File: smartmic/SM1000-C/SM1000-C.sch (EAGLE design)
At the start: 175 parts, among them CN1 HDR100-3, CN10 MJ-3523-SMT, CN11 HDR100-3, CN12 DF11-16DS, CN2 MOLEX-MINI-B-SMT, CN3 RASM712PX, CN4 RJ-45, CN5 MJ-3523-SMT, CN6 MJ-3523-SMT, CN7 MJ-3523-SMT, CN8 MJ-3523-SMT, CN9 MJ-3523-SMT, J1 JMP-2PIN, J3 JMP-2PIN, J4 JMP-2PIN, J5 JMP-2PIN, P1 TPAD50, P10 TPAD50, P11 TPAD50, P12 TPAD50, P13 TPAD50, P14 TPAD50, P15 TPAD50, P16 TPAD50, P17 TPAD50, P18 TPAD50, P19 TPAD50, P2 TPAD50, P20 TPAD50, P3 TPAD50, P4 TPAD50, P5 TPAD50, P6 TPAD50, P7 TPAD50, P8 TPAD50, P9 TPAD50, SW1 SW-BOURNS-7914S, SW2 SW-BOURNS-7914S, SW3 DPDT, SW4 SW-BOURNS-7914S, T1 SM-LP-5001, T2 SM-LP-5001, U1 STM32F405, U2 LD3985M33R, U3 STMPS2141, U4 EMIF02-USB03F2, U5 TPS54329E, U6 LMV341, U7 LMV341, U8 LM386M-1, U9 LMV341

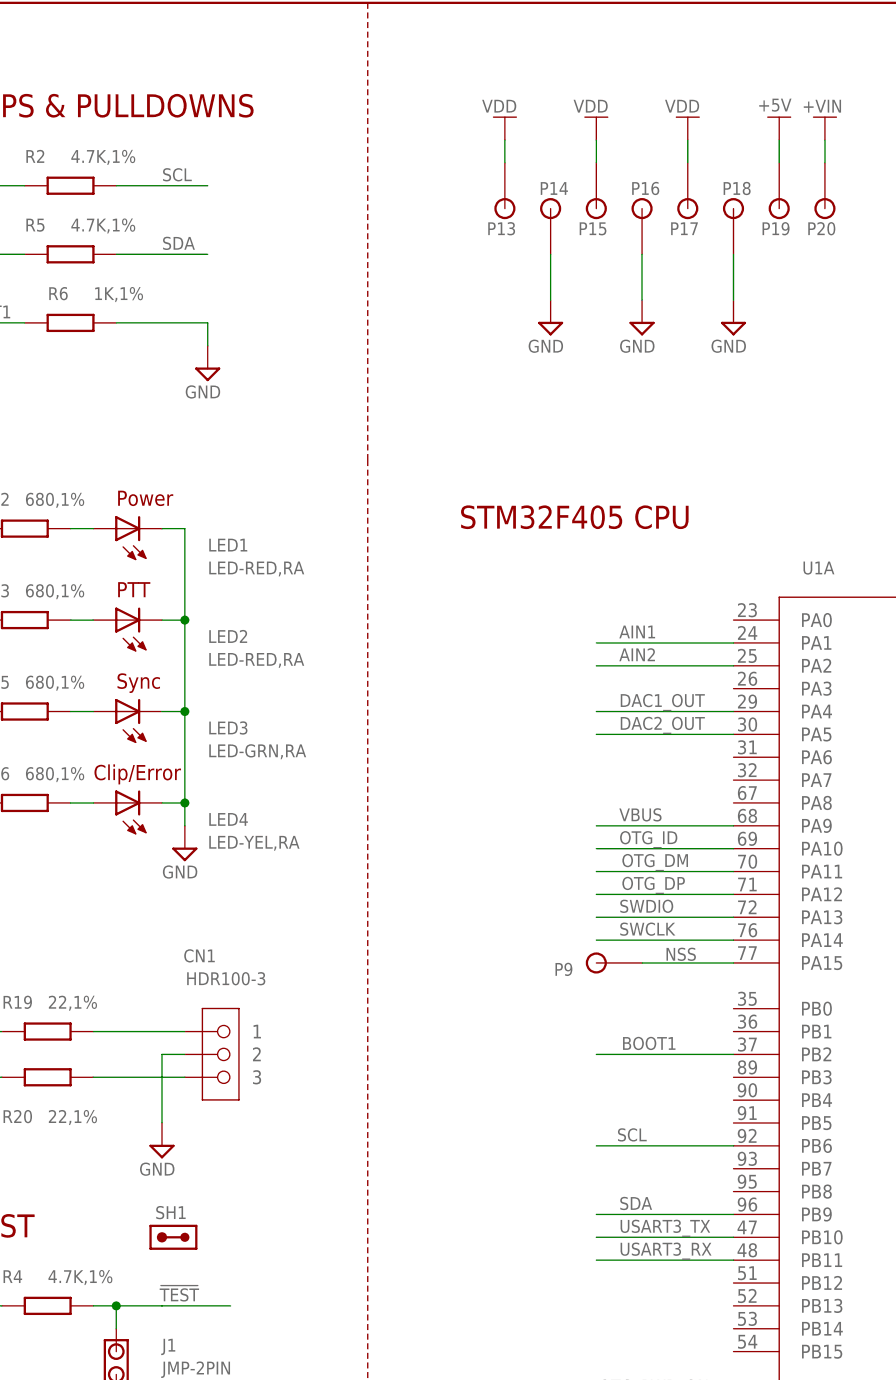
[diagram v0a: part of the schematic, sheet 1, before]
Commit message: Verifying Change-Log-C items 1-15 RGB
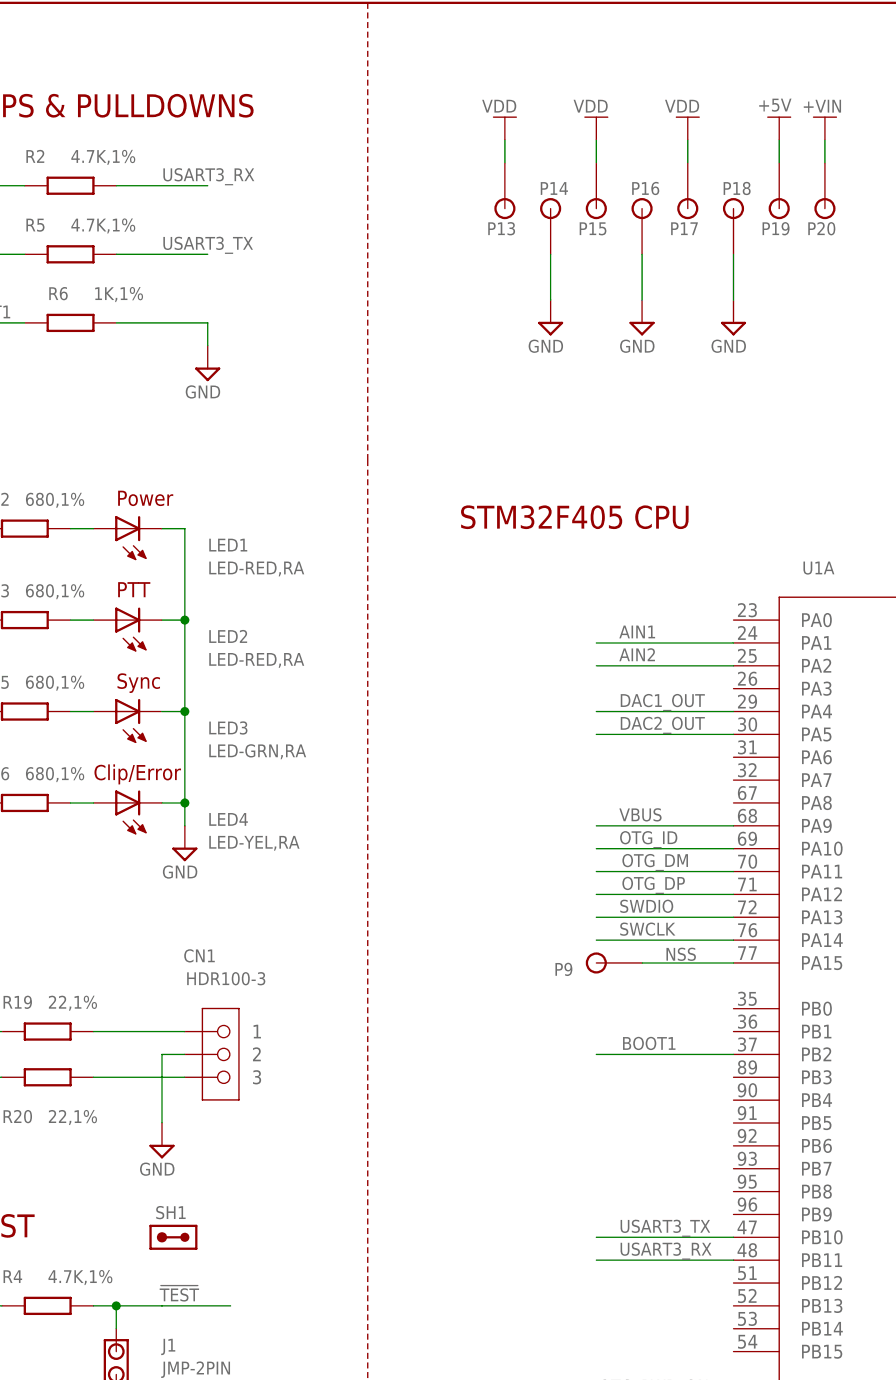
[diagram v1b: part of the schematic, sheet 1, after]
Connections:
- removed net SCL: R2.2, U1A.PB6
- removed net SDA: R5.2, U1A.PB9
- net USART3_RX: now also R2.2
- net USART3_TX: now also R5.2
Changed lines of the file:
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@@
-</segment>
-</net>
-<net name="SCL" class="0">
-<segment>
-<wire x1="104.14" y1="152.4" x2="88.9" y2="152.4" width="0.1524" layer="91"/>
-<label x="91.186" y="152.908" size="1.4224" layer="95" ratio="10"/>
-<pinref part="U1" gate="A" pin="PB6"/>
-</segment>
-<segment>
-<pinref part="R2" gate="G$1" pin="2"/>
-<wire x1="35.56" y1="259.08" x2="45.72" y2="259.08" width="0.1524" layer="91"/>
-<label x="40.64" y="259.588" size="1.4224" layer="95" ratio="10"/>
-</segment>
-</net>
-<net name="SDA" class="0">
-<segment>
-<wire x1="104.14" y1="144.78" x2="88.9" y2="144.78" width="0.1524" layer="91"/>
-<label x="91.44" y="145.288" size="1.4224" layer="95" ratio="10"/>
-<pinref part="U1" gate="A" pin="PB9"/>
-</segment>
-<segment>
-<pinref part="R5" gate="G$1" pin="2"/>
-<wire x1="35.56" y1="251.46" x2="45.72" y2="251.46" width="0.1524" layer="91"/>
-<label x="40.64" y="251.968" size="1.4224" layer="95" ratio="10"/>
 </segment>
 </net>
@@
 <label x="91.44" y="140.208" size="1.4224" layer="95" ratio="10"/>
 </segment>
+<segment>
+<pinref part="R2" gate="G$1" pin="2"/>
+<wire x1="35.56" y1="259.08" x2="45.72" y2="259.08" width="0.1524" layer="91"/>
+<label x="40.64" y="259.588" size="1.4224" layer="95" ratio="10"/>
+</segment>
 </net>
 <net name="USART3_TX" class="0">
@@
 <label x="91.44" y="142.748" size="1.4224" layer="95" ratio="10"/>
 </segment>
-</net>
+<segment>
+<pinref part="R5" gate="G$1" pin="2"/>
+<wire x1="35.56" y1="251.46" x2="45.72" y2="251.46" width="0.1524" layer="91"/>
+<label x="40.64" y="251.968" size="1.4224" layer="95" ratio="10"/>
+</segment>
+</net>

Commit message: Update to reflect review of Change-Log-C.txt  RGB 09/08/2014
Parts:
- added C54: 1nF,16V, AA-ipc-7351-capacitor:CAPACITOR_0603
- added R23: 10K,1%, AA-ipc-7351-resistor:RESISTOR_0603
- R39: value 22.1K,1% -> 2.21K,1%
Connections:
- removed net N$81: R47.3, R49.2
- new net N$13: R47.1, R49.2
- new net N$14: R23.2, R43.1, U6.-IN
- net AIN1: now also R23.1; no longer R43.1, U6.-IN
- net AIN2: now also C54.2, R42.1; no longer R42.3
- net N$41: now also C54.1, R42.3; no longer R42.1
- net N$82: now also R47.3; no longer R47.1
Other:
- moved on the sheet: P4, R47
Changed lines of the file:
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@@
 <part name="V56" library="A-SUPPLY2" deviceset="GND" device=""/>
 <part name="C34" library="AA-ipc-7351-capacitor" deviceset="CAPACITOR_" device="0603" value="1nF,25V"/>
-<part name="R39" library="AA-ipc-7351-resistor" deviceset="RESISTOR_" device="0603" value="22.1K,1%"/>
+<part name="R39" library="AA-ipc-7351-resistor" deviceset="RESISTOR_" device="0603" value="2.21K,1%"/>
 <part name="R40" library="AA-ipc-7351-resistor" deviceset="RESISTOR_" device="0603" value="2.2K,1%"/>
 <part name="V59" library="A-SUPPLY2" deviceset="GND" device=""/>
@@
 <part name="R22" library="AA-ipc-7351-resistor" deviceset="RESISTOR_" device="0603" value="22.1K,1%"/>
 <part name="V125" library="A-SUPPLY2" deviceset="GND" device=""/>
+<part name="C54" library="AA-ipc-7351-capacitor" deviceset="CAPACITOR_" device="0603" value="1nF,16V"/>
+<part name="R23" library="AA-ipc-7351-resistor" deviceset="RESISTOR_" device="0603" value="10K,1%"/>
 </parts>
 <sheets>
@@
 </instance>
 <instance part="B-FRAME3" gate="G$3" x="355.6" y="279.4" smashed="yes"/>
-<instance part="R47" gate="G$1" x="238.76" y="88.9" smashed="yes">
-<attribute name="NAME" x="233.68" y="86.36" size="1.4224" layer="95" ratio="9" rot="R90"/>
-<attribute name="VALUE" x="236.22" y="86.36" size="1.4224" layer="96" ratio="9" rot="R90"/>
+<instance part="R47" gate="G$1" x="238.76" y="88.9" smashed="yes" rot="MR180">
+<attribute name="NAME" x="233.68" y="91.44" size="1.4224" layer="95" ratio="9" rot="MR270"/>
+<attribute name="VALUE" x="236.22" y="91.44" size="1.4224" layer="96" ratio="9" rot="MR270"/>
 </instance>
 <instance part="R52" gate="G$1" x="226.06" y="132.08" smashed="yes" rot="R180">
@@
 <attribute name="VALUE" x="93.98" y="134.62" size="1.4224" layer="96" ratio="9"/>
 </instance>
-<instance part="R42" gate="G$1" x="116.84" y="147.32" smashed="yes" rot="R90">
-<attribute name="NAME" x="124.46" y="152.4" size="1.4224" layer="95" ratio="9"/>
-<attribute name="VALUE" x="124.46" y="149.86" size="1.4224" layer="96" ratio="9"/>
+<instance part="R42" gate="G$1" x="116.84" y="147.32" smashed="yes" rot="MR90">
+<attribute name="NAME" x="114.3" y="157.48" size="1.4224" layer="95" ratio="9" rot="MR0"/>
+<attribute name="VALUE" x="114.3" y="152.4" size="1.4224" layer="96" ratio="9" rot="MR0"/>
 </instance>
 <instance part="V62" gate="GND" x="99.06" y="109.22" smashed="yes">
@@
 <instance part="P2" gate="G$1" x="170.18" y="83.82" rot="R180"/>
 <instance part="P3" gate="G$1" x="27.94" y="71.12"/>
-<instance part="P4" gate="G$1" x="129.54" y="127" rot="R180"/>
+<instance part="P4" gate="G$1" x="132.08" y="127" rot="R180"/>
 <instance part="C1" gate="G$1" x="101.6" y="251.46" smashed="yes" rot="R90">
 <attribute name="NAME" x="96.52" y="266.7" size="1.4224" layer="95"/>
@@
 <attribute name="VALUE" x="25.4" y="47.498" size="1.4224" layer="96" ratio="9"/>
 </instance>
+<instance part="C54" gate="G$1" x="124.46" y="154.94" smashed="yes">
+<attribute name="NAME" x="127" y="157.48" size="1.4224" layer="95"/>
+<attribute name="VALUE" x="121.92" y="149.86" size="1.4224" layer="96"/>
+</instance>
+<instance part="R23" gate="G$1" x="187.96" y="147.32" smashed="yes">
+<attribute name="NAME" x="182.88" y="149.86" size="1.4224" layer="95" ratio="9"/>
+<attribute name="VALUE" x="187.96" y="149.86" size="1.4224" layer="96" ratio="9"/>
+</instance>
 </instances>
 <busses>
@@
 <segment>
 <label x="132.588" y="130.302" size="1.4224" layer="95" ratio="10"/>
-<wire x1="129.54" y1="129.54" x2="137.16" y2="129.54" width="0.1524" layer="91"/>
+<wire x1="132.08" y1="129.54" x2="137.16" y2="129.54" width="0.1524" layer="91"/>
 <pinref part="U9" gate="G$1" pin="OUT"/>
-<wire x1="124.46" y1="129.54" x2="129.54" y2="129.54" width="0.1524" layer="91"/>
-<pinref part="R42" gate="G$1" pin="3"/>
-<wire x1="124.46" y1="147.32" x2="129.54" y2="147.32" width="0.1524" layer="91"/>
-<wire x1="129.54" y1="147.32" x2="129.54" y2="129.54" width="0.1524" layer="91"/>
-<wire x1="129.54" y1="127" x2="129.54" y2="129.54" width="0.1524" layer="91"/>
+<wire x1="124.46" y1="129.54" x2="132.08" y2="129.54" width="0.1524" layer="91"/>
+<wire x1="132.08" y1="147.32" x2="132.08" y2="129.54" width="0.1524" layer="91"/>
+<wire x1="132.08" y1="127" x2="132.08" y2="129.54" width="0.1524" layer="91"/>
 <pinref part="P4" gate="G$1" pin="1"/>
-<junction x="129.54" y="129.54"/>
+<junction x="132.08" y="129.54"/>
+<pinref part="C54" gate="G$1" pin="2"/>
+<wire x1="129.54" y1="154.94" x2="132.08" y2="154.94" width="0.1524" layer="91"/>
+<wire x1="132.08" y1="154.94" x2="132.08" y2="147.32" width="0.1524" layer="91"/>
+<pinref part="R42" gate="G$1" pin="1"/>
+<wire x1="124.46" y1="147.32" x2="132.08" y2="147.32" width="0.1524" layer="91"/>
+<junction x="132.08" y="147.32"/>
 </segment>
 </net>
@@
 <wire x1="177.8" y1="129.54" x2="170.18" y2="129.54" width="0.1524" layer="91"/>
 <wire x1="170.18" y1="127" x2="170.18" y2="129.54" width="0.1524" layer="91"/>
-<pinref part="U6" gate="G$1" pin="-IN"/>
-<wire x1="193.04" y1="132.08" x2="195.58" y2="132.08" width="0.1524" layer="91"/>
-<pinref part="R43" gate="G$1" pin="1"/>
-<wire x1="195.58" y1="132.08" x2="198.12" y2="132.08" width="0.1524" layer="91"/>
-<wire x1="195.58" y1="132.08" x2="195.58" y2="147.32" width="0.1524" layer="91"/>
-<wire x1="195.58" y1="147.32" x2="170.18" y2="147.32" width="0.1524" layer="91"/>
-<junction x="195.58" y="132.08"/>
 <wire x1="170.18" y1="129.54" x2="170.18" y2="147.32" width="0.1524" layer="91"/>
 <pinref part="P1" gate="G$1" pin="1"/>
 <junction x="170.18" y="129.54"/>
+<pinref part="R23" gate="G$1" pin="1"/>
+<wire x1="170.18" y1="147.32" x2="182.88" y2="147.32" width="0.1524" layer="91"/>
 </segment>
 </net>
@@
 </segment>
 </net>
-<net name="N$81" class="0">
-<segment>
-<pinref part="R49" gate="G$1" pin="2"/>
-<pinref part="R47" gate="G$1" pin="3"/>
-<wire x1="238.76" y1="78.74" x2="238.76" y2="81.28" width="0.1524" layer="91"/>
-</segment>
-</net>
 <net name="N$82" class="0">
 <segment>
-<pinref part="R47" gate="G$1" pin="1"/>
-<wire x1="238.76" y1="96.52" x2="238.76" y2="99.06" width="0.1524" layer="91"/>
 <pinref part="R48" gate="G$1" pin="1"/>
 <wire x1="238.76" y1="99.06" x2="236.22" y2="99.06" width="0.1524" layer="91"/>
+<pinref part="R47" gate="G$1" pin="3"/>
+<wire x1="238.76" y1="96.52" x2="238.76" y2="99.06" width="0.1524" layer="91"/>
 </segment>
 </net>
@@
 </segment>
 </net>
-<net name="N$61" class="0">
-<segment>
-<pinref part="R47" gate="G$1" pin="2"/>
-<pinref part="C47" gate="G$1" pin="1"/>
-<wire x1="243.84" y1="88.9" x2="246.38" y2="88.9" width="0.1524" layer="91"/>
-</segment>
-</net>
 <net name="N$79" class="0">
 <segment>
@@
 <net name="N$41" class="0">
 <segment>
-<wire x1="106.68" y1="147.32" x2="109.22" y2="147.32" width="0.1524" layer="91"/>
-<pinref part="R42" gate="G$1" pin="1"/>
-<pinref part="R42" gate="G$1" pin="2"/>
-<wire x1="116.84" y1="152.4" x2="116.84" y2="154.94" width="0.1524" layer="91"/>
 <wire x1="116.84" y1="154.94" x2="106.68" y2="154.94" width="0.1524" layer="91"/>
 <wire x1="106.68" y1="154.94" x2="106.68" y2="147.32" width="0.1524" layer="91"/>
 <pinref part="R53" gate="G$1" pin="2"/>
 <wire x1="106.68" y1="144.78" x2="106.68" y2="147.32" width="0.1524" layer="91"/>
+<pinref part="C54" gate="G$1" pin="1"/>
+<wire x1="116.84" y1="154.94" x2="119.38" y2="154.94" width="0.1524" layer="91"/>
+<pinref part="R42" gate="G$1" pin="2"/>
+<wire x1="116.84" y1="152.4" x2="116.84" y2="154.94" width="0.1524" layer="91"/>
+<pinref part="R42" gate="G$1" pin="3"/>
+<wire x1="109.22" y1="147.32" x2="106.68" y2="147.32" width="0.1524" layer="91"/>
 <junction x="106.68" y="147.32"/>
+<junction x="116.84" y="154.94"/>
 </segment>
 </net>
@@
 </segment>
 </net>
+<net name="N$11" class="0">
+<segment>
+<pinref part="R47" gate="G$1" pin="2"/>
+<pinref part="C47" gate="G$1" pin="1"/>
+<wire x1="243.84" y1="88.9" x2="246.38" y2="88.9" width="0.1524" layer="91"/>
+</segment>
+</net>
+<net name="N$13" class="0">
+<segment>
+<pinref part="R47" gate="G$1" pin="1"/>
+<pinref part="R49" gate="G$1" pin="2"/>
+<wire x1="238.76" y1="81.28" x2="238.76" y2="78.74" width="0.1524" layer="91"/>
+</segment>
+</net>
+<net name="N$14" class="0">
+<segment>
+<pinref part="R43" gate="G$1" pin="1"/>
+<wire x1="195.58" y1="132.08" x2="198.12" y2="132.08" width="0.1524" layer="91"/>
+<wire x1="195.58" y1="132.08" x2="195.58" y2="147.32" width="0.1524" layer="91"/>
+<junction x="195.58" y="132.08"/>
+<pinref part="U6" gate="G$1" pin="-IN"/>
+<wire x1="193.04" y1="132.08" x2="195.58" y2="132.08" width="0.1524" layer="91"/>
+<pinref part="R23" gate="G$1" pin="2"/>
+<wire x1="193.04" y1="147.32" x2="195.58" y2="147.32" width="0.1524" layer="91"/>
+</segment>
+</net>

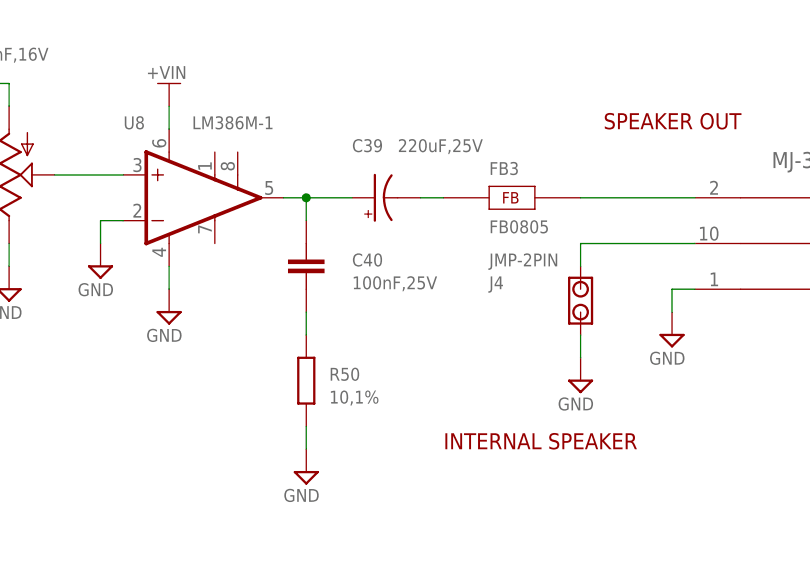
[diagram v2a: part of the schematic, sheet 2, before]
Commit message: Update SNN with Change-Log-C.txt changes. RGB 09/10/2014
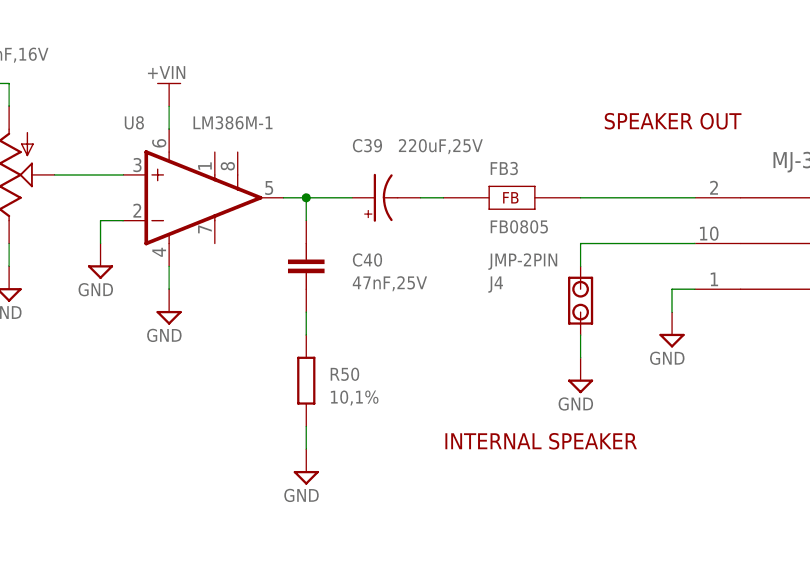
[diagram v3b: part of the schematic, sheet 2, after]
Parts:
- C40: value 100nF,25V -> 47nF,25V
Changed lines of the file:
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@@
 <part name="V64" library="A-SUPPLY2" deviceset="GND" device=""/>
 <part name="U$8" library="A-SUPPLY2" deviceset="+VIN" device=""/>
-<part name="C40" library="AA-ipc-7351-capacitor" deviceset="CAPACITOR_" device="0603" value="100nF,25V"/>
+<part name="C40" library="AA-ipc-7351-capacitor" deviceset="CAPACITOR_" device="0603" value="47nF,25V"/>
 <part name="R50" library="AA-ipc-7351-resistor" deviceset="RESISTOR_" device="0603" value="10,1%"/>
 <part name="V65" library="A-SUPPLY2" deviceset="GND" device=""/>
